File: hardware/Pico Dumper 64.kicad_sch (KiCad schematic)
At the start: 1 part, among them U1 Pico

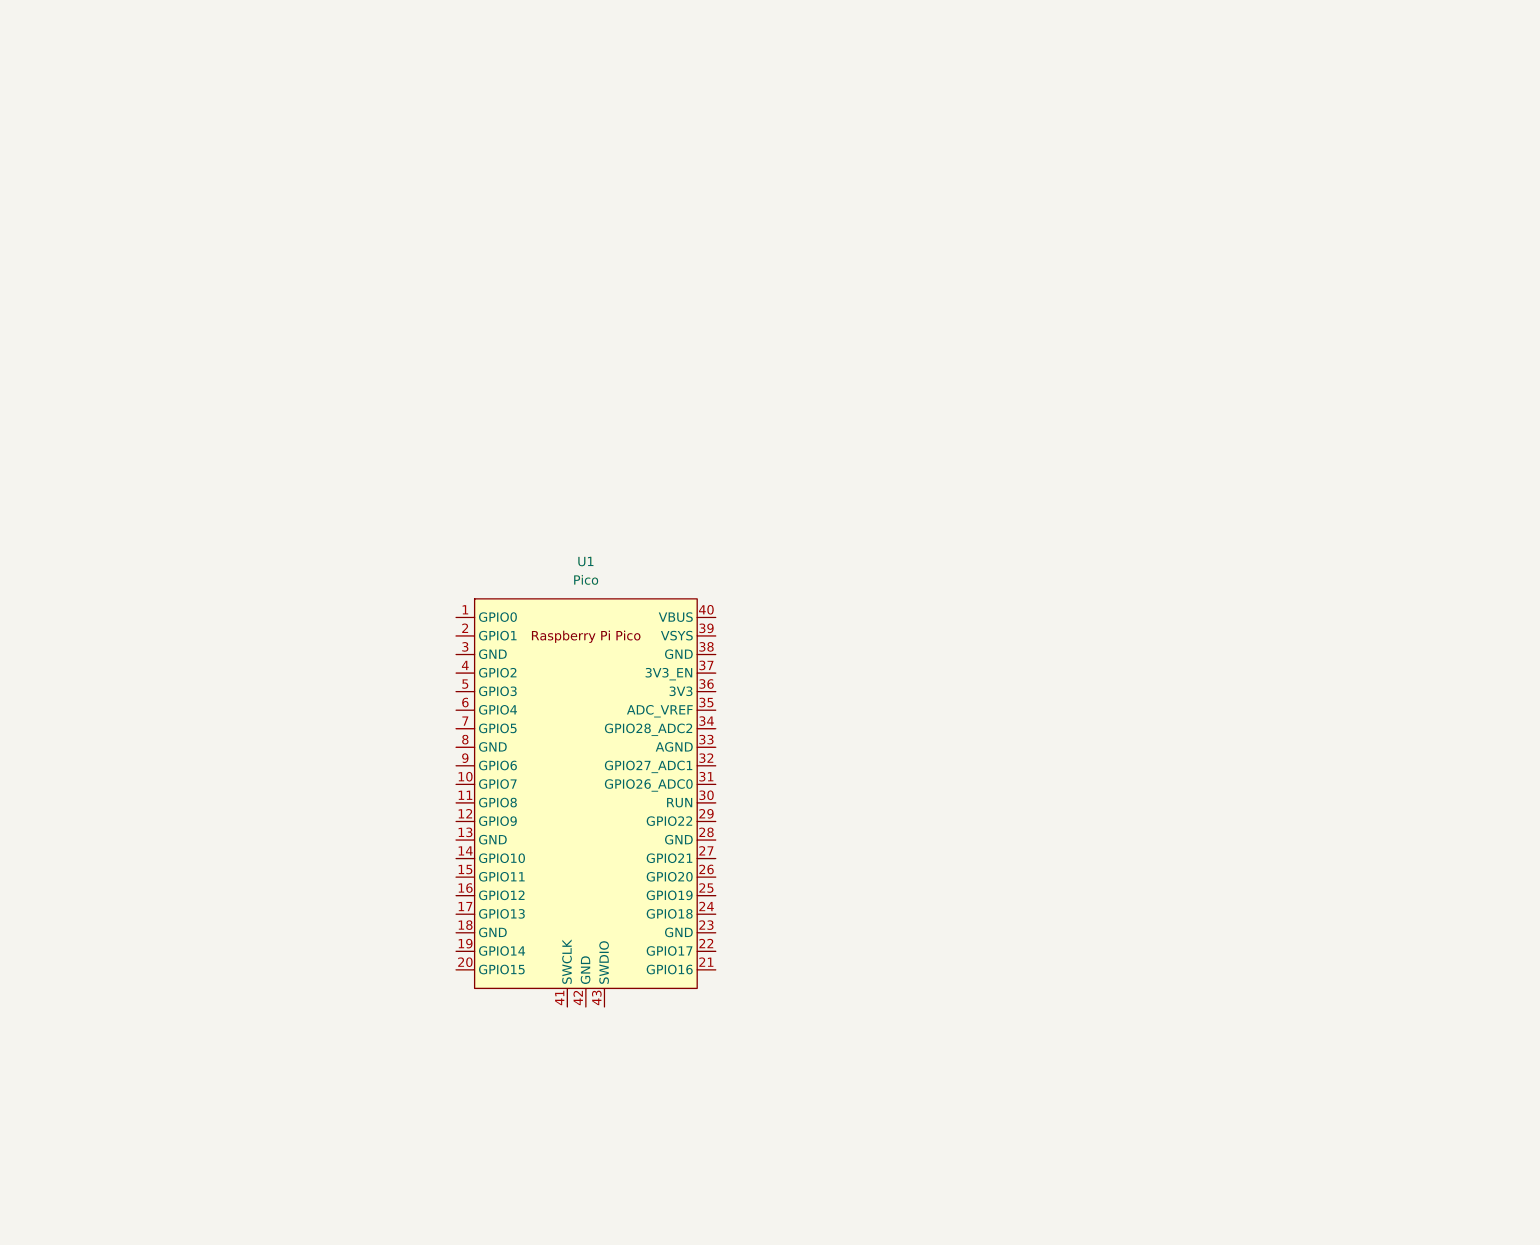
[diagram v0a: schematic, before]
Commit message: connect pico to cart slot on sch
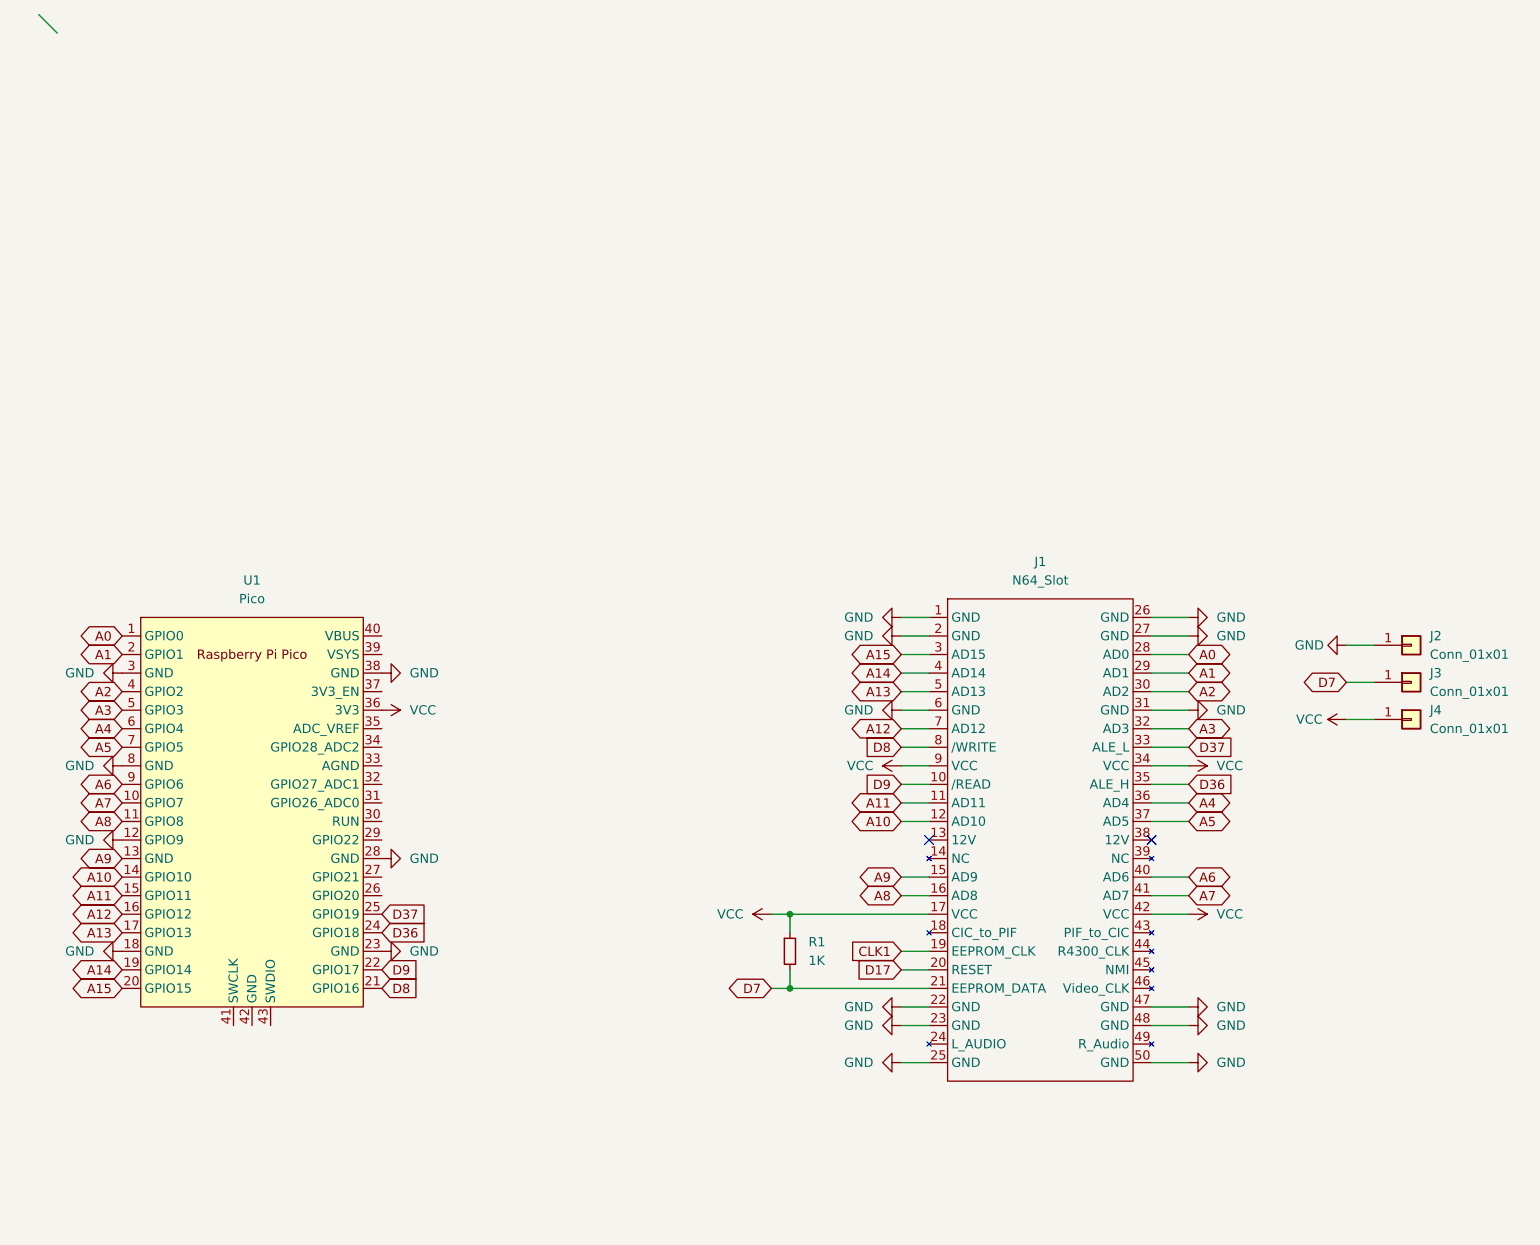
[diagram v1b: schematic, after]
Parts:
- added J1: N64_Slot, symbol sanni:N64_Slot
- added J2, J3, J4: Conn_01x01, symbol Connector_Generic:Conn_01x01
- added R1: 1K, symbol Device:R_Small
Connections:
- net A0: now reaches U1.1 (GPIO0)
- net A0: now also J1.28 (AD0)
- net A7: now reaches U1.10 (GPIO7)
- net A7: now also J1.41 (AD7)
- net A8: now reaches U1.11 (GPIO8)
- net A8: now also J1.16 (AD8)
- net GND: now reaches U1.12 (GPIO9)
- net GND: now also U1.18 (GND), U1.23 (GND), U1.28 (GND), U1.3 (GND), U1.38 (GND), U1.8 (GND), J1.1 (GND), J1.2 (GND), J1.22 (GND), J1.23 (GND), J1.25 (GND), J1.26 (GND), J1.27 (GND), J1.31 (GND), J1.47 (GND), J1.48 (GND), J1.50 (GND), J1.6 (GND), J2.1 (Pin_1)
- net A9: now reaches U1.13 (GND)
- net A9: now also J1.15 (AD9)
- net A10: now reaches U1.14 (GPIO10)
- net A10: now also J1.12 (AD10)
- net A11: now reaches U1.15 (GPIO11)
- net A11: now also J1.11 (AD11)
- net A12: now reaches U1.16 (GPIO12)
- net A12: now also J1.7 (AD12)
- net A13: now reaches U1.17 (GPIO13)
- net A13: now also J1.5 (AD13)
- net A14: now reaches U1.19 (GPIO14)
- net A14: now also J1.4 (AD14)
- net A1: now reaches U1.2 (GPIO1)
- net A1: now also J1.29 (AD1)
- net A15: now reaches U1.20 (GPIO15)
- net A15: now also J1.3 (AD15)
- net D8: now reaches U1.21 (GPIO16)
- net D8: now also J1.8 (/WRITE)
- net D9: now reaches U1.22 (GPIO17)
- net D9: now also J1.10 (/READ)
- net D36: now reaches U1.24 (GPIO18)
- net D36: now also J1.35 (ALE_H)
- net D37: now reaches U1.25 (GPIO19)
- net D37: now also J1.33 (ALE_L)
- net VCC: now reaches U1.36 (3V3)
- net VCC: now also J1.17 (VCC), J1.34 (VCC), J1.42 (VCC), J1.9 (VCC), J4.1 (Pin_1), R1.1
- net A2: now reaches U1.4 (GPIO2)
- net A2: now also J1.30 (AD2)
- net A3: now reaches U1.5 (GPIO3)
- net A3: now also J1.32 (AD3)
- net A4: now reaches U1.6 (GPIO4)
- net A4: now also J1.36 (AD4)
- net A5: now reaches U1.7 (GPIO5)
- net A5: now also J1.37 (AD5)
- net A6: now reaches U1.9 (GPIO6)
- net A6: now also J1.40 (AD6)
- new net CLK1: J1.19 (EEPROM_CLK)
- new net D17: J1.20 (RESET)
- new net D7: J1.21 (EEPROM_DATA), J3.1 (Pin_1), R1.2
- no-connect marks 0 -> 2
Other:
- moved on the sheet: U1

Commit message: update sch
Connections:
- net D17: now also U1.26 (GPIO20)
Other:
- moved on the sheet: J1, J2, J3, J4, R1, U1

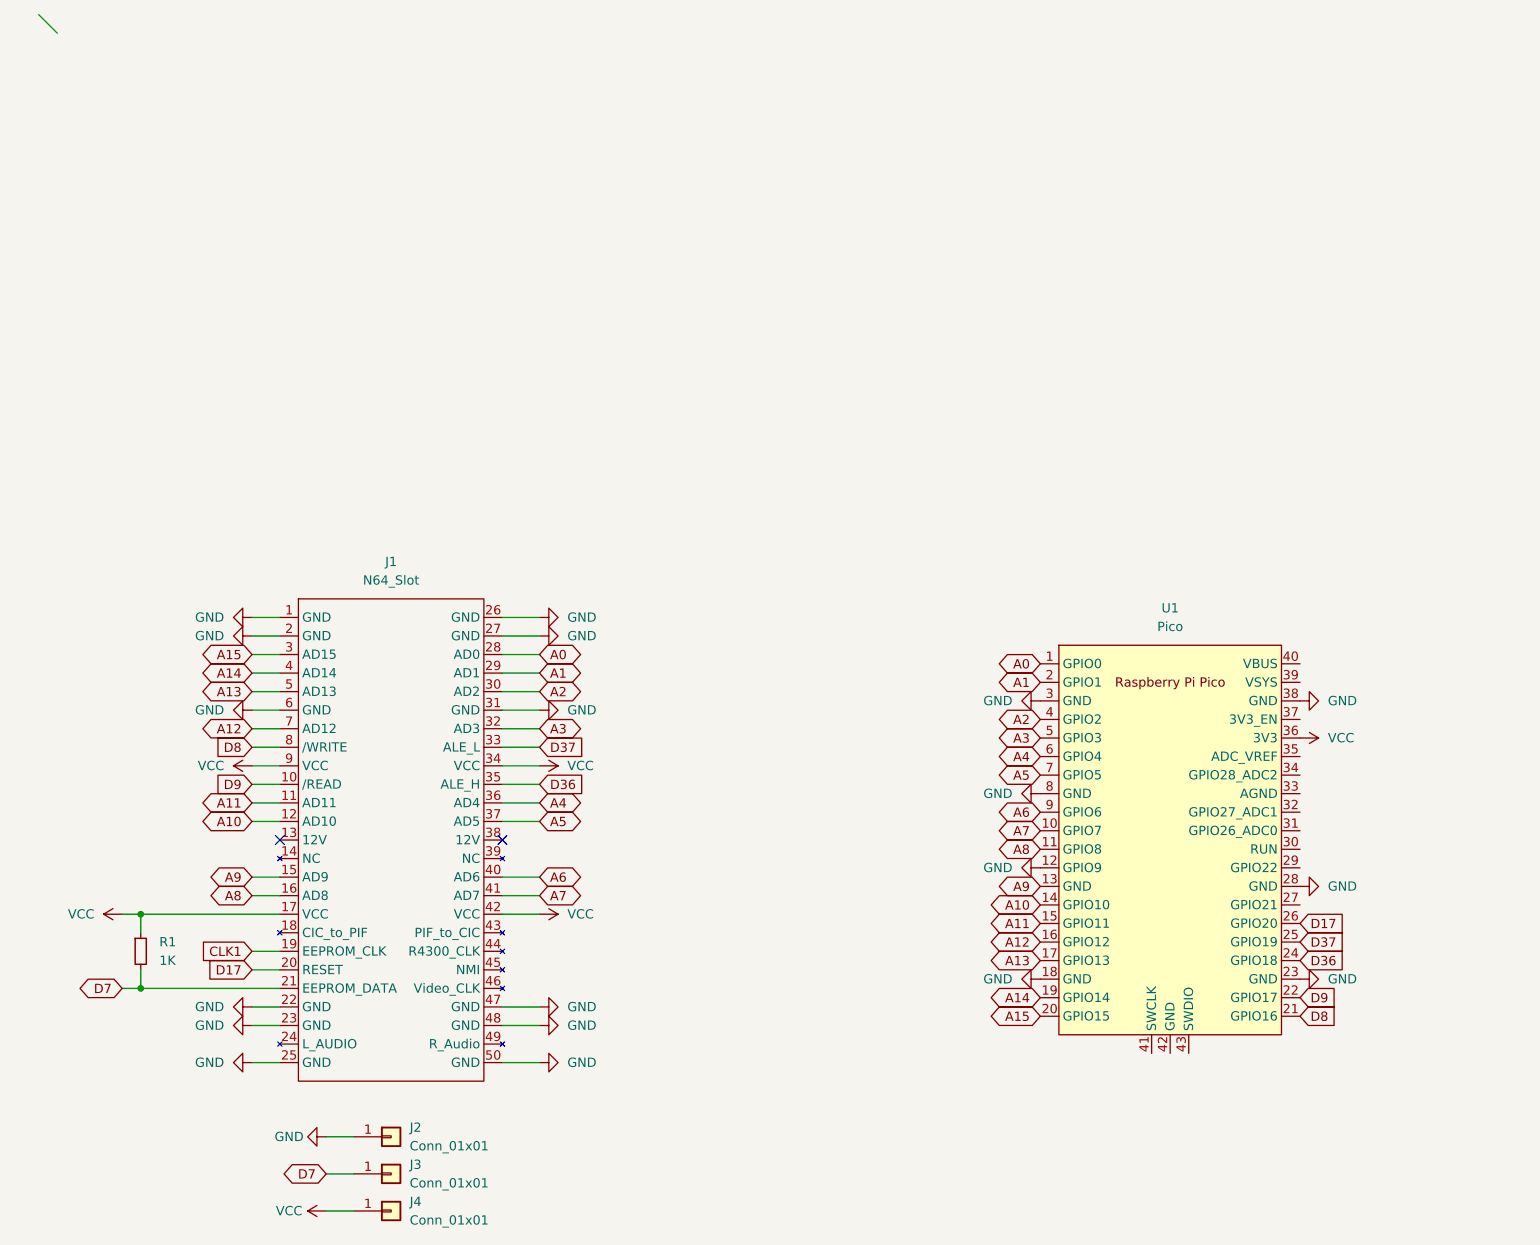
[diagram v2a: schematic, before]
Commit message: Add base n64 python version
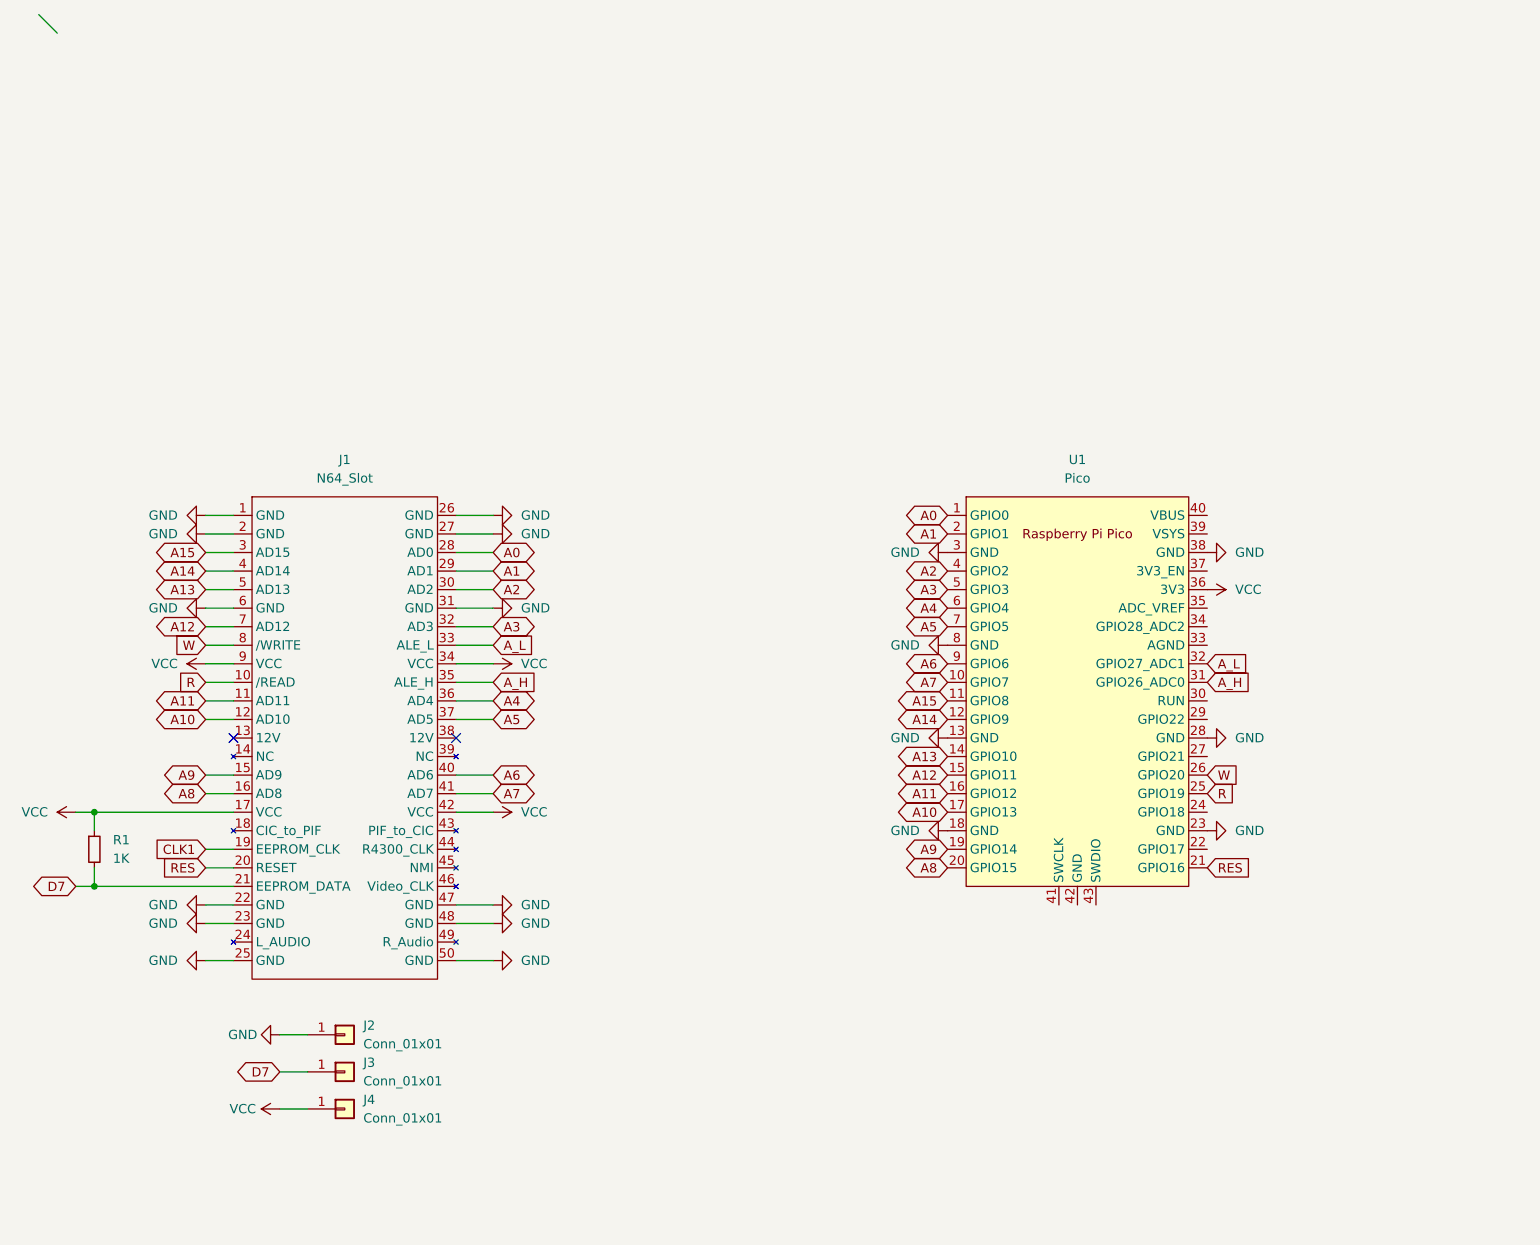
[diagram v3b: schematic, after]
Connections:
- net A10: now also U1.17 (GPIO13); no longer U1.14 (GPIO10)
- net A11: now also U1.16 (GPIO12); no longer U1.15 (GPIO11)
- net A12: now also U1.15 (GPIO11); no longer U1.16 (GPIO12)
- net A13: now also U1.14 (GPIO10); no longer U1.17 (GPIO13)
- net A14: now also U1.12 (GPIO9); no longer U1.19 (GPIO14)
- net A15: now also U1.11 (GPIO8); no longer U1.20 (GPIO15)
- net A8: now also U1.20 (GPIO15); no longer U1.11 (GPIO8)
- net A9: now also U1.19 (GPIO14); no longer U1.13 (GND)
- net GND: now also U1.13 (GND); no longer U1.12 (GPIO9)
- net A_H: now reaches U1.31 (GPIO26_ADC0)
- net A_H: now also J1.35 (ALE_H)
- net A_L: now reaches U1.32 (GPIO27_ADC1)
- net A_L: now also J1.33 (ALE_L)
- net D17 renamed RES
- net RES: now also U1.21 (GPIO16); no longer U1.26 (GPIO20)
- net D36: no longer names the net of U1.24 (GPIO18)
- net D36: no longer J1.35 (ALE_H)
- net D37 renamed R
- net R: now also J1.10 (/READ); no longer J1.33 (ALE_L)
- net D8 renamed W
- net W: now also U1.26 (GPIO20); no longer U1.21 (GPIO16)
- net D9: no longer names the net of U1.22 (GPIO17)
- net D9: no longer J1.10 (/READ)
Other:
- moved on the sheet: J1, J2, J3, J4, R1, U1
